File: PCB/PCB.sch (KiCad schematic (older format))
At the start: 17 parts, among them J1 Conn_01x04_Male, P1 Power, P2 Analog, P3 Digital, P4 Digital, P5 CONN_01X01, P6 CONN_01X01, P7 CONN_01X01, P8 CONN_01X01, U1 LM393

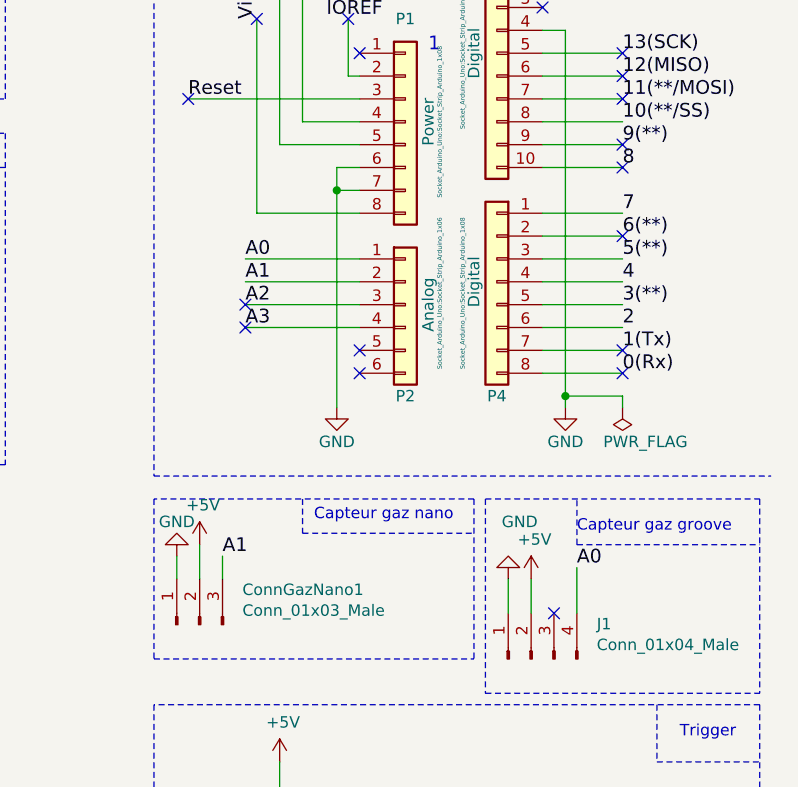
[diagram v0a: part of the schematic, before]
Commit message: ajout pcb capteur nano et maj pcb shield
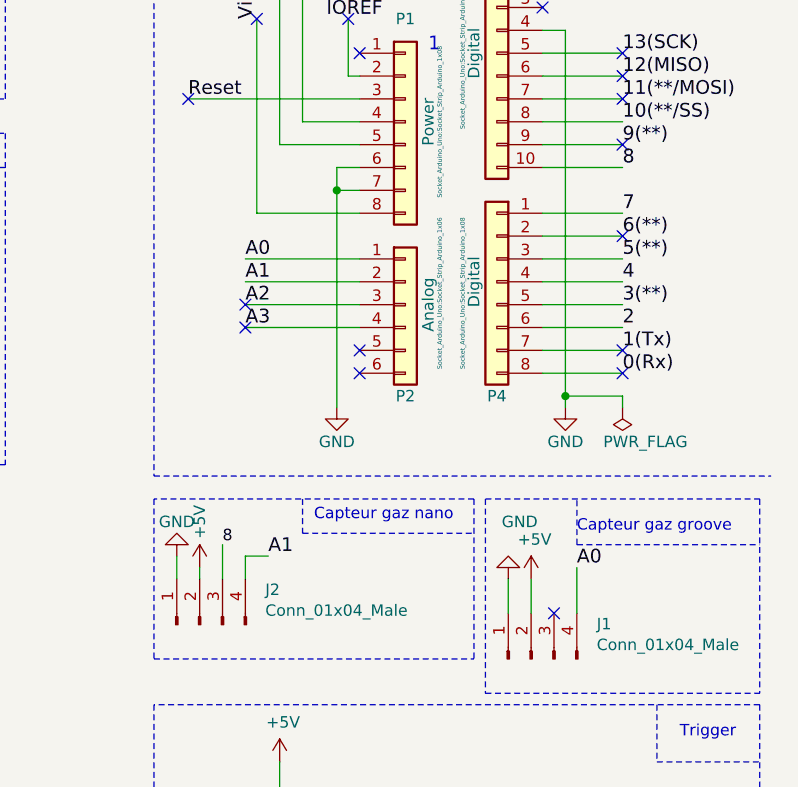
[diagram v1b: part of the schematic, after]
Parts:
- removed ConnGazNano1: Conn_01x03_Male, Connector_PinHeader_2.54mm:PinHeader_1x03_P2.54mm_Vertical, symbol Connector:Conn_01x03_Male
- added J2: Conn_01x04_Male, Connector_PinSocket_2.54mm:PinSocket_1x04_P2.54mm_Vertical, symbol Connector:Conn_01x04_Male
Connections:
- net +5V: now also J2.2 (Pin_2)
- net 8: now also J2.3 (Pin_3)
- net A1: now also J2.4 (Pin_4)
- net GND: now also J2.1 (Pin_1)
- no-connect marks 27 -> 26
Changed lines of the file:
@@
 Text Label 10550 2300 0    60   ~ 0
 7
-Text Label 10550 2100 0    60   ~ 0
-8
 Text Label 10550 2000 0    60   ~ 0
 9(**)
@@
 Wire Notes Line
 	10350 3750 11150 3750
-$Comp
-L Connector:Conn_01x03_Male ConnGazNano1
-U 1 1 5BC7F9BF
-P 8700 4100
-F 0 "ConnGazNano1" V 8853 3913 50  0000 R CNN
-F 1 "Conn_01x03_Male" V 8762 3913 50  0000 R CNN
-F 2 "Connector_PinHeader_2.54mm:PinHeader_1x03_P2.54mm_Vertical" H 8700 4100 50  0001 C CNN
-F 3 "~" H 8700 4100 50  0001 C CNN
-	1    8700 4100
-	0    -1   -1   0
-$EndComp
 Wire Notes Line
 	9900 3550 8500 3550
@@
 	-1   0    0    1
 $EndComp
-$Comp
-L power:+5V #PWR07
-U 1 1 5BCB267F
-P 8700 3750
-F 0 "#PWR07" H 8700 3600 50  0001 C CNN
-F 1 "+5V" H 8715 3923 50  0000 C CNN
-F 2 "" H 8700 3750 50  0001 C CNN
-F 3 "" H 8700 3750 50  0001 C CNN
-	1    8700 3750
-	1    0    0    -1
-$EndComp
-Wire Wire Line
-	8700 3750 8700 3900
+Wire Wire Line
+	8700 3850 8700 3900
 Wire Wire Line
 	8600 3800 8600 3900
-Wire Wire Line
-	8800 3900 8800 3800
-Text Label 8800 3800 0    60   ~ 0
+Text Label 9000 3800 0    60   ~ 0
 A1
 NoConn ~ 8650 1800
@@
 NoConn ~ 8950 1450
 NoConn ~ 10550 2400
-NoConn ~ 10550 2100
 NoConn ~ 10550 2000
 NoConn ~ 10550 1800
@@
 	10100 5850 9050 5850
 Connection ~ 9050 5850
+$Comp
+L Connector:Conn_01x04_Male J2
+U 1 1 5BE15EA1
+P 8700 4100
+F 0 "J2" V 8853 3813 50  0000 R CNN
+F 1 "Conn_01x04_Male" V 8762 3813 50  0000 R CNN
+F 2 "Connector_PinSocket_2.54mm:PinSocket_1x04_P2.54mm_Vertical" H 8700 4100 50  0001 C CNN
+F 3 "~" H 8700 4100 50  0001 C CNN
+	1    8700 4100
+	0    -1   -1   0
+$EndComp
+Text Label 10550 2100 0    60   ~ 0
+8
+Wire Wire Line
+	9000 3800 8900 3800
+Wire Wire Line
+	8900 3800 8900 3900
+Text Label 8800 3750 0    50   ~ 0
+8
+Wire Wire Line
+	8800 3750 8800 3900
+$Comp
+L power:+5V #PWR?
+U 1 1 5BE17B03
+P 8700 3850
+F 0 "#PWR?" H 8700 3700 50  0001 C CNN
+F 1 "+5V" V 8700 4050 50  0000 C CNN
+F 2 "" H 8700 3850 50  0000 C CNN
+F 3 "" H 8700 3850 50  0000 C CNN
+	1    8700 3850
+	1    0    0    -1
+$EndComp
 $EndSCHEMATC
